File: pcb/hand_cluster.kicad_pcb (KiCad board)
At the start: 2 copper layers, 159.2 x 110 mm, 72 parts, among them J1 AudioJack4, J2 AudioJack4, U1 ProMicro

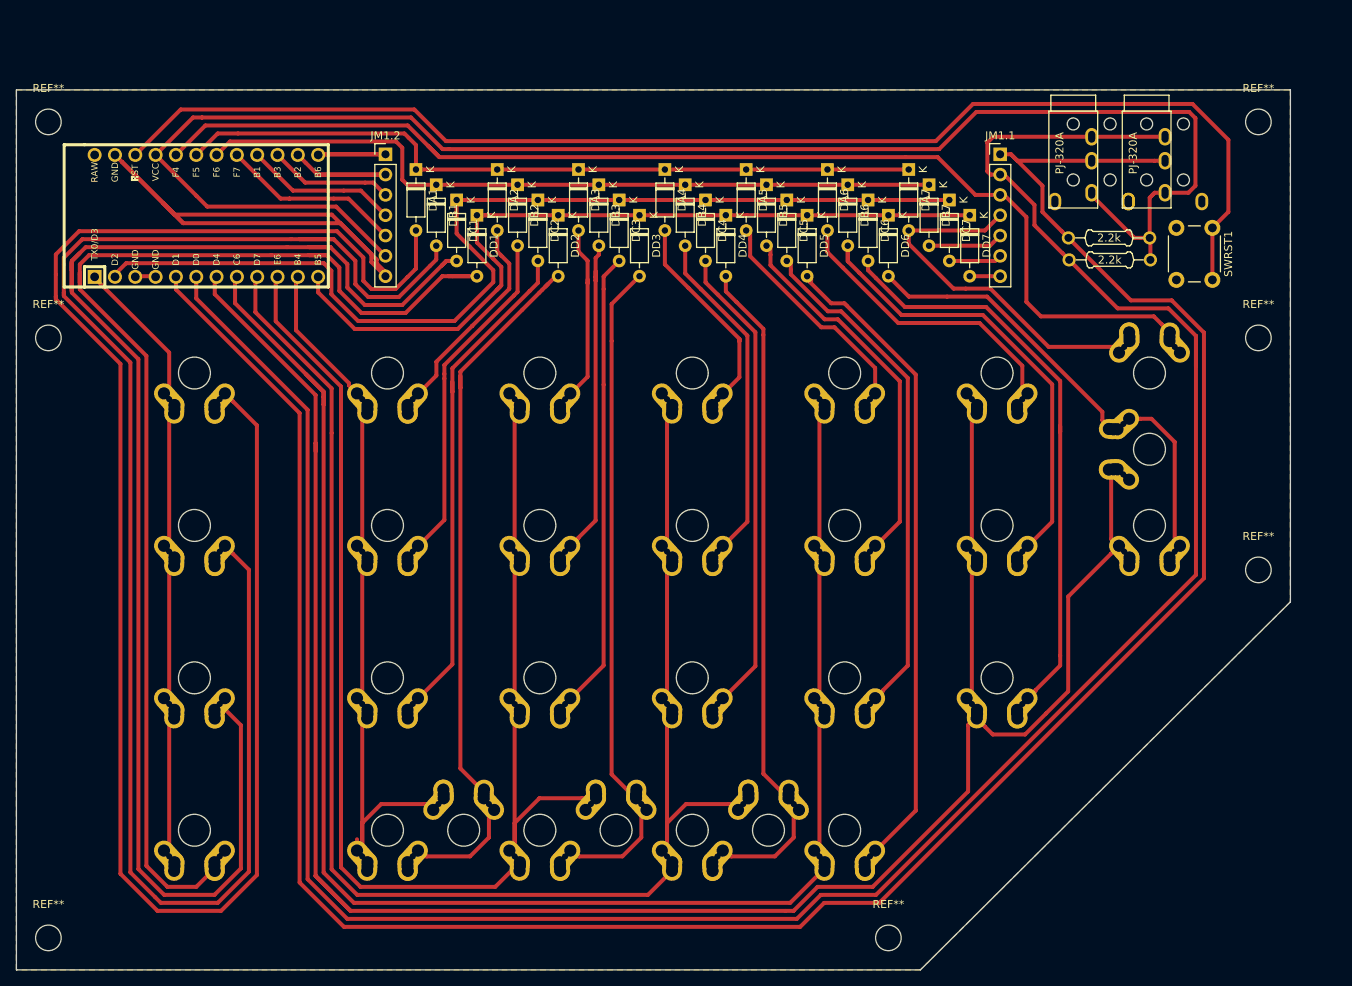
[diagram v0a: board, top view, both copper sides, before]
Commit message: Modified the main pcb hand cluster to a near completed prototype design
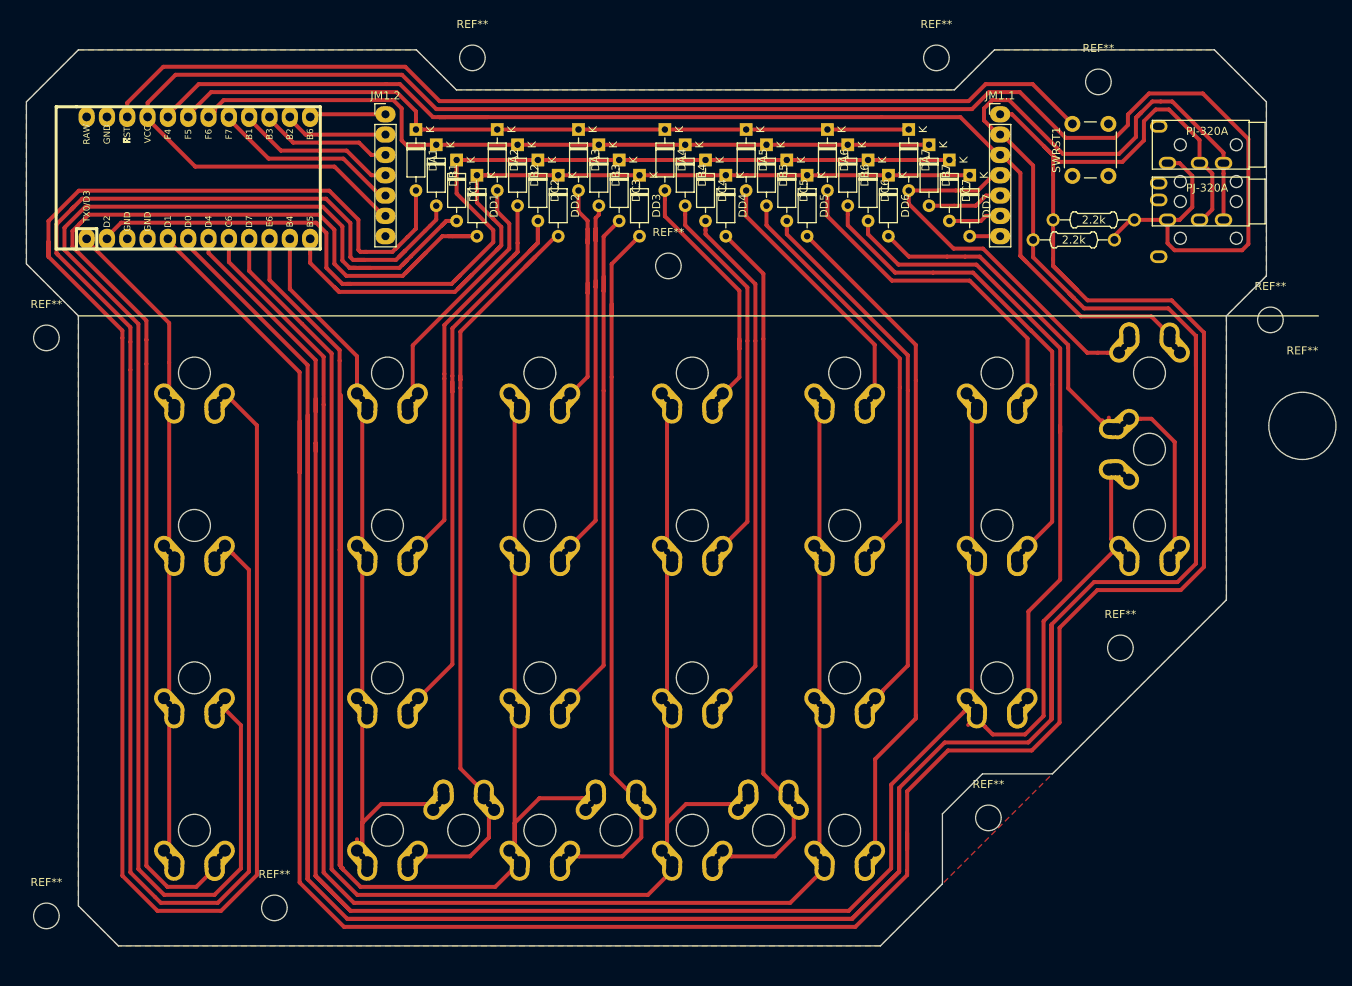
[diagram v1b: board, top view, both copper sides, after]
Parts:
- removed the REF** at (274.0, -30.1)
- removed the REF** at (274.0, -1.10)
- removed the REF** at (274.0, -57.1)
- removed the REF** at (122.7, -57.1)
- removed the REF** at (122.7, -30.1)
- added REF**: MountingHole_8.4mm_M8, MountingHole:MountingHole_8.4mm_M8, F.Cu at (279.5, -19.1)
- added REF**: MountingHole_3.2mm_M3, MountingHole:MountingHole_3.2mm_M3, F.Cu at (233.7, -65.1)
- added REF**: MountingHole_3.2mm_M3, MountingHole:MountingHole_3.2mm_M3, F.Cu at (175.7, -65.1)
- added REF**: MountingHole_3.2mm_M3, MountingHole:MountingHole_3.2mm_M3, F.Cu at (240.2, 29.9)
- added REF**: MountingHole_3.2mm_M3, MountingHole:MountingHole_3.2mm_M3, F.Cu at (275.5, -32.4)
- added REF**: MountingHole_3.2mm_M3, MountingHole:MountingHole_3.2mm_M3, F.Cu at (122.5, -30.1)
- added REF**: MountingHole_3.2mm_M3, MountingHole:MountingHole_3.2mm_M3, F.Cu at (122.5, 42.1)
- added REF**: MountingHole_3.2mm_M3, MountingHole:MountingHole_3.2mm_M3, F.Cu at (200.2, -39.1)
- added REF**: MountingHole_3.2mm_M3, MountingHole:MountingHole_3.2mm_M3, F.Cu at (254.0, -62.1)
- moved REF** 46.4 mm to (256.7, 8.64)
- moved REF** 28.5 mm to (151.0, 41.1)
- moved J2 20.7 mm to (272.8, -51.9), turned to 270 degrees
- moved SWRST1 18.7 mm to (250.7, -50.4), turned to 90 degrees
- moved J1 17.2 mm to (272.8, -44.9), turned to 270 degrees
- moved R2 5.15 mm to (250.9, -42.4)
- moved DA1 5.00 mm to (168.7, -56.1)
- moved DA2 5.00 mm to (178.8, -56.1)
- moved DA3 5.00 mm to (189.0, -56.1)
- moved DA4 5.00 mm to (199.8, -56.1)
- moved DA5 5.00 mm to (210.0, -56.1)
- moved DA6 5.00 mm to (220.1, -56.1)
- moved DA7 5.00 mm to (230.3, -56.1)
- moved DB1 5.00 mm to (171.2, -54.2)
- moved DB2 5.00 mm to (181.4, -54.2)
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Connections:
- net Enc1A renamed Ard18_Analog
- net Enc1B renamed Ard15_SCLK
- net Enc2A renamed Ard14_MISO
- net Enc2B renamed Ard16_MOSI
- net Unused renamed Ard10_Analog
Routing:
- net SDA: track 307.3 -> 540.5 mm
- net GND: track 86.7 -> 0.00 mm
- net Col3: track 174.7 -> 239.1 mm
- net SCL: track 302.4 -> 358.8 mm
- net Reset: track 162.7 -> 126.5 mm
- net VCC: track 202.6 -> 233.2 mm
- net Col6: track 275.0 -> 284.4 mm
- net Col7: track 144.7 -> 154.1 mm
- net Net-(DC2-Pad2): track 63.1 -> 72.3 mm
- net Net-(DA3-Pad2): track 23.2 -> 31.2 mm
- net Net-(DA1-Pad2): track 221.4 -> 229.3 mm
- net Ard16_MOSI: track 21.0 -> 13.3 mm
- net Ard10_Analog: track 17.3 -> 9.66 mm
- net Net-(DD6-Pad2): track 57.0 -> 64.3 mm
- net Net-(DC3-Pad2): track 58.2 -> 65.0 mm
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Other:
- board size 159.2 x 110 mm -> 155 x 112 mm
